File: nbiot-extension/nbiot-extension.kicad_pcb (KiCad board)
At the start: 2 copper layers, 2 parts, among them J1 SIM_Card_Shielded, U1 BC66NB-04-STD

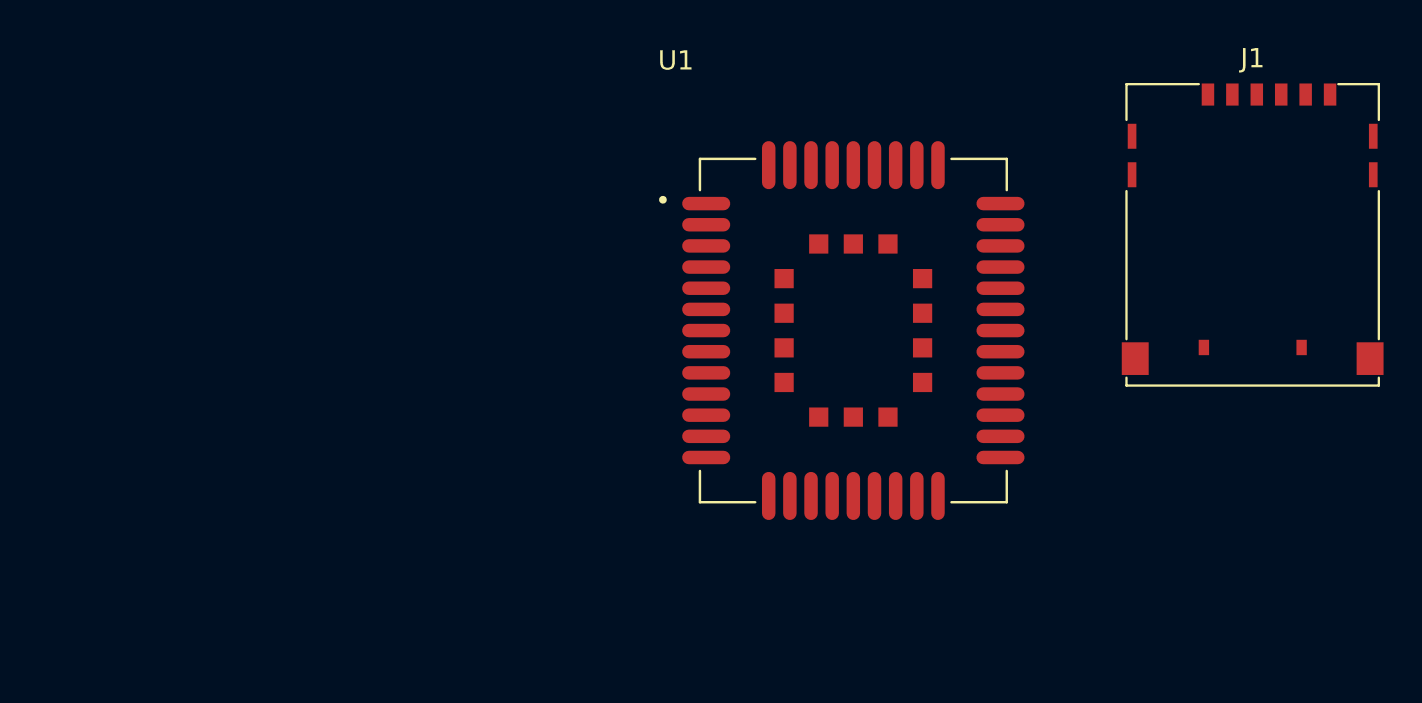
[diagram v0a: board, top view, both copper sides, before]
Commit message: Feature/kicad 6 migration (#2)
* Adjust CI/CD jobs to use KiCad 6

* Migrate panel module project

* Unify KiBot config

* Migrate Ethernet, SoC, Metering Modules to KiCad6

* Change build order to find out more about strange behavior

* Trigger build also on workflow changes

* Try to increase log level to track error

* Switch to KiCad 6 schematic files

* Fix / Ignore Errors in panel module

* Disable cost calculation for now

* Fixing more ERC errors

* Remove outdated files and settings

* Trim further warnings and errors

* Update documentation

* Migrate in-progress projects
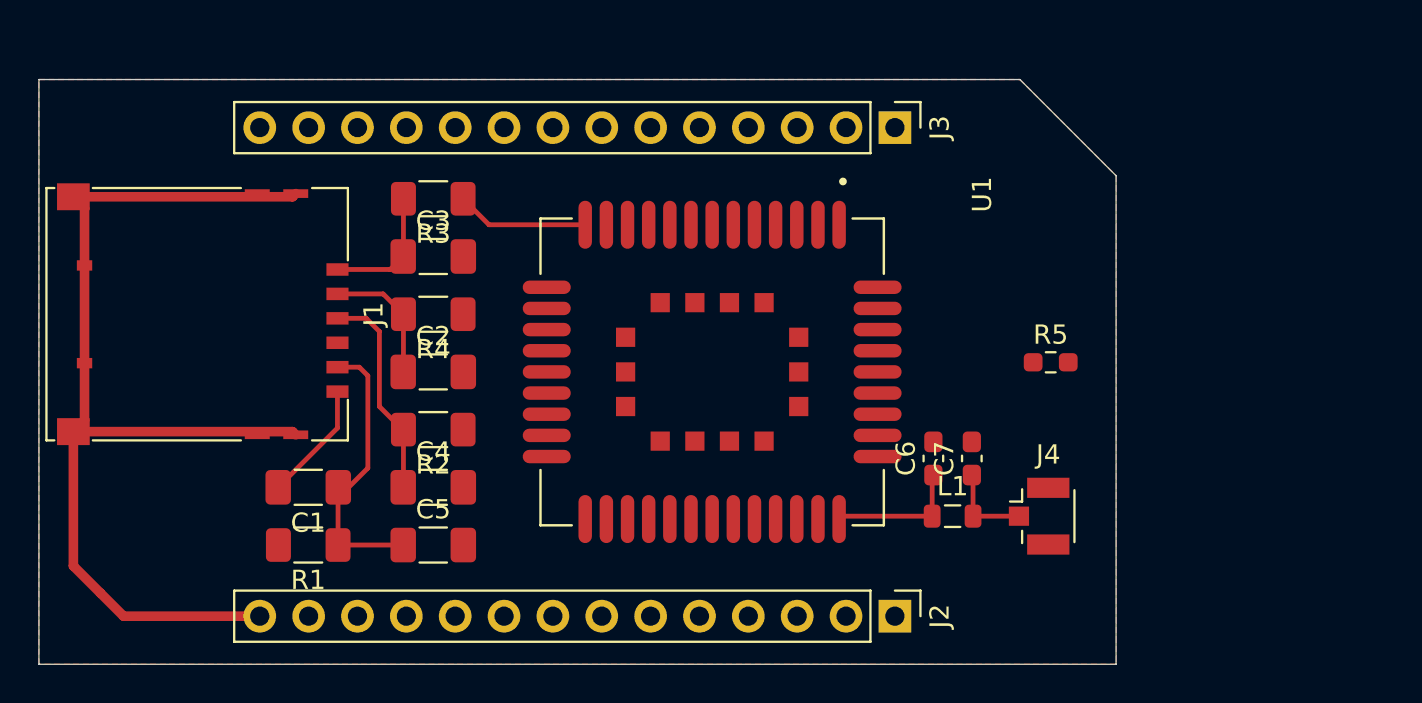
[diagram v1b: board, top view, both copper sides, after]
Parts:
- added C1: 100nF, Capacitor_SMD:C_1206_3216Metric_Pad1.33x1.80mm_HandSolder, F.Cu at (114.0, 101.0)
- added C2: 33pF, Capacitor_SMD:C_1206_3216Metric_Pad1.33x1.80mm_HandSolder, F.Cu at (120.5, 95.0)
- added C3: 33pF, Capacitor_SMD:C_1206_3216Metric_Pad1.33x1.80mm_HandSolder, F.Cu at (120.5, 89.0)
- added C4: 33pF, Capacitor_SMD:C_1206_3216Metric_Pad1.33x1.80mm_HandSolder, F.Cu at (120.5, 101.0)
- added C5: 33pF, Capacitor_SMD:C_1206_3216Metric_Pad1.33x1.80mm_HandSolder, F.Cu at (120.5, 104.0)
- added C6: 0F, Capacitor_SMD:C_0603_1608Metric_Pad1.08x0.95mm_HandSolder, F.Cu at (146.5, 99.5)
- added C7: 0F, Capacitor_SMD:C_0603_1608Metric_Pad1.08x0.95mm_HandSolder, F.Cu at (148.5, 99.5)
- added J2: East, Connector_PinHeader_2.54mm:PinHeader_1x14_P2.54mm_Vertical, F.Cu at (144.5, 107.7)
- added J3: West, Connector_PinHeader_2.54mm:PinHeader_1x14_P2.54mm_Vertical, F.Cu at (144.5, 82.3)
- added J4: Conn_Coaxial, Connector_Coaxial:U.FL_Hirose_U.FL-R-SMT-1_Vertical, F.Cu at (152.0, 102.5)
- added L1: L, Inductor_SMD:L_0805_2012Metric, F.Cu at (147.5, 102.5)
- added R1: 10k, Resistor_SMD:R_1206_3216Metric_Pad1.30x1.75mm_HandSolder, F.Cu at (114.0, 104.0)
- added R2: 22R, Resistor_SMD:R_1206_3216Metric_Pad1.30x1.75mm_HandSolder, F.Cu at (120.5, 98.0)
- added R3: 22R, Resistor_SMD:R_1206_3216Metric_Pad1.30x1.75mm_HandSolder, F.Cu at (120.5, 86.0)
- added R4: 22R, Resistor_SMD:R_1206_3216Metric_Pad1.30x1.75mm_HandSolder, F.Cu at (120.5, 92.0)
- added R5: 0R, Resistor_SMD:R_0603_1608Metric_Pad0.98x0.95mm_HandSolder, F.Cu at (152.6, 94.5)
- moved J1 54.4 mm to (108.9, 92.0), turned to -90 degrees
- moved U1 7.65 mm to (135.0, 95.0), turned to -90 degrees
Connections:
- net Net-(U1-Pad1) renamed GND
- J1 pad 1: Net-(J1-Pad1) -> SIM_VDD
- J1 pad 5: Net-(J1-Pad5) -> SIM_GND
- J1 pad 6: Net-(J1-Pad6) -> unconnected-(J1-Pad6)
- J1 pad SH: Net-(J1-PadSH) -> GNDPWR
- U1 pad 10: Net-(U1-Pad10) -> SIM_GND
- U1 pad 11: Net-(U1-Pad11) -> SIM_DATA
- U1 pad 12: Net-(U1-Pad12) -> SIM_RST
- U1 pad 13: Net-(U1-Pad13) -> SIM_CLK
- U1 pad 14: Net-(U1-Pad14) -> SIM_VDD
- U1 pad 15: Net-(U1-Pad15) -> unconnected-(U1-Pad15)
- U1 pad 16: Net-(U1-Pad16) -> unconnected-(U1-Pad16)
- U1 pad 17: Net-(U1-Pad17) -> unconnected-(U1-Pad17)
- U1 pad 18: Net-(U1-Pad18) -> unconnected-(U1-Pad18)
- U1 pad 19: Net-(U1-Pad19) -> unconnected-(U1-Pad19)
- U1 pad 20: Net-(U1-Pad20) -> unconnected-(U1-Pad20)
- U1 pad 24: Net-(U1-Pad24) -> unconnected-(U1-Pad24)
- U1 pad 28: Net-(U1-Pad28) -> unconnected-(U1-Pad28)
- U1 pad 29: Net-(U1-Pad29) -> unconnected-(U1-Pad29)
- U1 pad 35: Net-(U1-Pad35) -> ANTENNA
- U1 pad 38: Net-(U1-Pad38) -> unconnected-(U1-Pad38)
- U1 pad 39: Net-(U1-Pad39) -> unconnected-(U1-Pad39)
- U1 pad 42: Net-(U1-Pad42) -> unconnected-(U1-Pad42)
- U1 pad 43: Net-(U1-Pad43) -> unconnected-(U1-Pad43)
- U1 pad 47: Net-(U1-Pad47) -> unconnected-(U1-Pad47)
- U1 pad 49: Net-(U1-Pad49) -> unconnected-(U1-Pad49)
- U1 pad 50: Net-(U1-Pad50) -> unconnected-(U1-Pad50)
- U1 pad 51: Net-(U1-Pad51) -> unconnected-(U1-Pad51)
- U1 pad 7: Net-(U1-Pad7) -> unconnected-(U1-Pad7)
- U1 pad 9: Net-(U1-Pad9) -> unconnected-(U1-Pad9)
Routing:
- net GNDPWR: track 0.00 -> 53.7 mm
- net SIM_VDD: track 0.00 -> 14.9 mm
- net Net-(C4-Pad1): track 0.00 -> 11.1 mm
- net ANTENNA: track 0.00 -> 7.06 mm
- net SIM_CLK: track 0.00 -> 6.91 mm
- net Net-(C2-Pad1): track 0.00 -> 6.87 mm
- net Net-(C3-Pad1): track 0.00 -> 6.70 mm
- net SIM_GND: track 0.00 -> 6.25 mm
- net Net-(C7-Pad1): track 0.00 -> 4.55 mm
- added copper zone on F.Cu, net GND
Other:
- board outline added: 56 x 30.4 mm
- net class Default removed
